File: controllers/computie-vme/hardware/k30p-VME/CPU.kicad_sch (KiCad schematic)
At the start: 18 parts, among them SW1 ~{RESET}, U1 MC68030RC, U2 74HC14, U3 74HC05

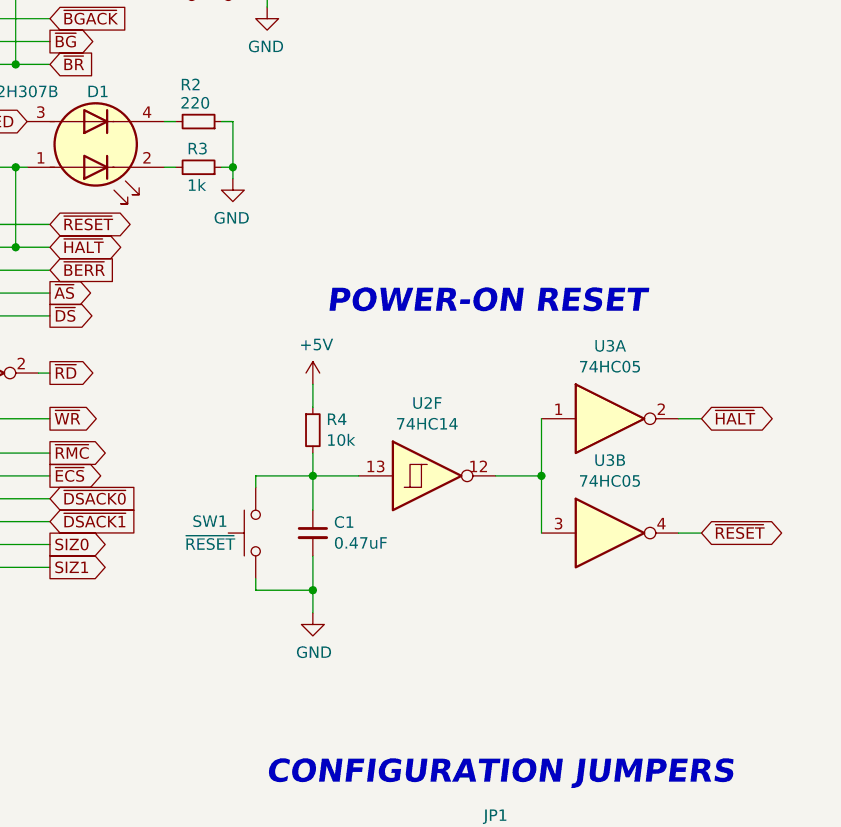
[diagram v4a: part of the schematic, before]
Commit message: Schematics for k30p-VME more or less done
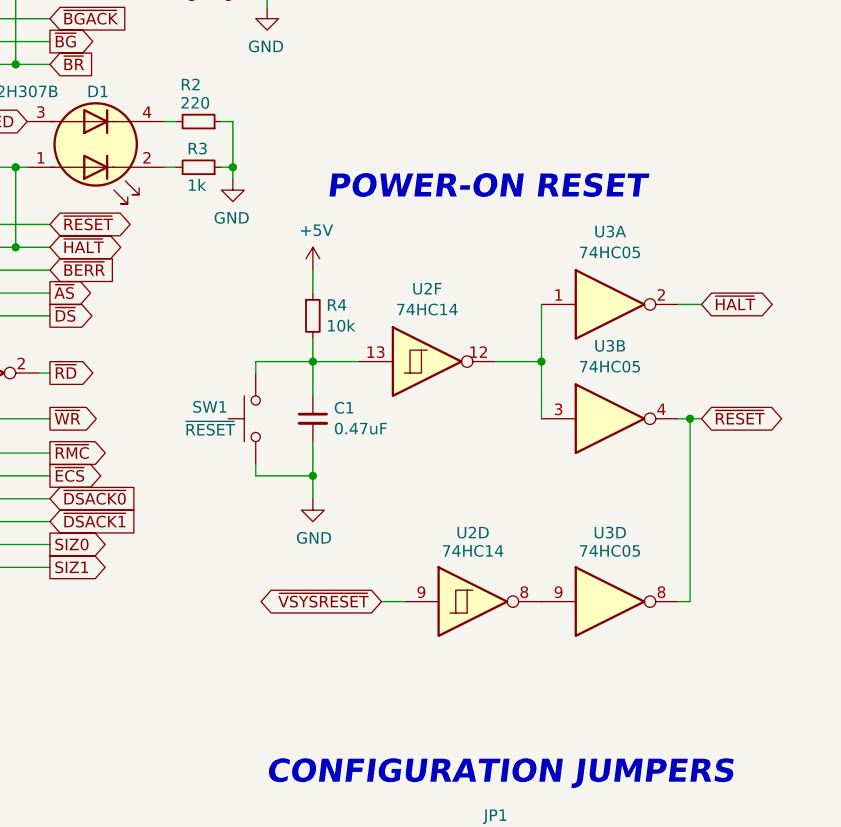
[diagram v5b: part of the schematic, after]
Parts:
- added unit 4 of U2
- added unit 4 of U3
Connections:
- net ~{RESET}: now also U3.8
- new net: U2.8, U3.9
- new net ~{VSYSRESET}: U2.9
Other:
- moved on the sheet: C1, R4, SW1, U2F, U3A, U3B

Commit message: WIP on k30p-VME
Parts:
- removed TP2: IPEND, TestPoint:TestPoint_THTPad_2.0x2.0mm_Drill1.0mm, symbol Connector:TestPoint
- removed TP3: REFILL, TestPoint:TestPoint_THTPad_2.0x2.0mm_Drill1.0mm, symbol Connector:TestPoint
- removed TP4: STATUS, TestPoint:TestPoint_THTPad_2.0x2.0mm_Drill1.0mm, symbol Connector:TestPoint
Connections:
- no-connect marks 5 -> 8
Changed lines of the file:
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@@
 	)
 	(no_connect
+		(at 125.73 142.24)
+	)
+	(no_connect
+		(at 125.73 40.64)
+	)
+	(no_connect
+		(at 125.73 144.78)
+	)
+	(no_connect
 		(at 125.73 100.33)
 	)
@@
 	)
 	(symbol
-		(lib_id "Connector:TestPoint")
-		(at 125.73 40.64 270)
-		(unit 1)
-		(exclude_from_sim no)
-		(in_bom yes)
-		(on_board yes)
-		(dnp no)
-		(property "Reference" "TP2"
-			(at 133.35 40.64 90)
-			(effects
-				(font
-					(size 1.27 1.27)
-				)
-				(justify right)
-			)
-		)
-		(property "Value" "IPEND"
-			(at 127 38.1 90)
-			(effects
-				(font
-					(size 1.27 1.27)
-				)
-				(justify left)
-			)
-		)
-		(property "Footprint" "TestPoint:TestPoint_THTPad_2.0x2.0mm_Drill1.0mm"
-			(at 125.73 45.72 0)
-			(effects
-				(font
-					(size 1.27 1.27)
-				)
-				(hide yes)
-			)
-		)
-		(property "Datasheet" "~"
-			(at 125.73 45.72 0)
-			(effects
-				(font
-					(size 1.27 1.27)
-				)
-				(hide yes)
-			)
-		)
-		(property "Description" ""
-			(at 125.73 40.64 0)
-			(effects
-				(font
-					(size 1.27 1.27)
-				)
-				(hide yes)
-			)
-		)
-		(pin "1"
-		)
-		(instances
-			(project "IVC-k30"
-				(path "/dd13a6b9-cb24-4a73-96ce-c29930072fba/dfc443dd-7c5d-4956-9c53-a8ea419d150b"
-					(reference "TP2")
-					(unit 1)
-				)
-			)
-			(project "k30-SBC"
-				(path "/fc911c32-ec9d-4dc3-a64d-23ac8e8e7030"
-					(reference "TP1")
-					(unit 1)
-				)
-			)
-		)
-	)
-	(symbol
 		(lib_id "Device:R_Small")
 		(at 217.17 60.96 270)
@@
 	)
 	(symbol
-		(lib_id "Connector:TestPoint")
-		(at 125.73 142.24 270)
-		(unit 1)
-		(exclude_from_sim no)
-		(in_bom yes)
-		(on_board yes)
-		(dnp no)
-		(property "Reference" "TP3"
-			(at 133.35 142.24 90)
-			(effects
-				(font
-					(size 1.27 1.27)
-				)
-				(justify right)
-			)
-		)
-		(property "Value" "REFILL"
-			(at 133.35 142.24 90)
-			(effects
-				(font
-					(size 1.27 1.27)
-				)
-				(justify left)
-			)
-		)
-		(property "Footprint" "TestPoint:TestPoint_THTPad_2.0x2.0mm_Drill1.0mm"
-			(at 125.73 147.32 0)
-			(effects
-				(font
-					(size 1.27 1.27)
-				)
-				(hide yes)
-			)
-		)
-		(property "Datasheet" "~"
-			(at 125.73 147.32 0)
-			(effects
-				(font
-					(size 1.27 1.27)
-				)
-				(hide yes)
-			)
-		)
-		(property "Description" ""
-			(at 125.73 142.24 0)
-			(effects
-				(font
-					(size 1.27 1.27)
-				)
-				(hide yes)
-			)
-		)
-		(pin "1"
-		)
-		(instances
-			(project "IVC-k30"
-				(path "/dd13a6b9-cb24-4a73-96ce-c29930072fba/dfc443dd-7c5d-4956-9c53-a8ea419d150b"
-					(reference "TP3")
-					(unit 1)
-				)
-			)
-			(project "k30-SBC"
-				(path "/fc911c32-ec9d-4dc3-a64d-23ac8e8e7030"
-					(reference "TP2")
-					(unit 1)
-				)
-			)
-		)
-	)
-	(symbol
 		(lib_id "Device:LED_Dual_AKAK")
 		(at 205.74 63.5 0)
@@
 					(unit 1)
 				)
-			)
-		)
-	)
-	(symbol
-		(lib_id "Connector:TestPoint")
-		(at 125.73 144.78 270)
-		(unit 1)
-		(exclude_from_sim no)
-		(in_bom yes)
-		(on_board yes)
-		(dnp no)
-		(property "Reference" "TP4"
-			(at 133.35 144.78 90)
-			(effects
-				(font
-					(size 1.27 1.27)
-				)
-				(justify right)
-			)
-		)
-		(property "Value" "STATUS"
-			(at 133.35 144.78 90)
-			(effects
-				(font
-					(size 1.27 1.27)
-				)
-				(justify left)
-			)
-		)
-		(property "Footprint" "TestPoint:TestPoint_THTPad_2.0x2.0mm_Drill1.0mm"
-			(at 125.73 149.86 0)
-			(effects
-				(font
-					(size 1.27 1.27)
-				)
-				(hide yes)
-			)
-		)
-		(property "Datasheet" "~"
-			(at 125.73 149.86 0)
-			(effects
-				(font
-					(size 1.27 1.27)
-				)
-				(hide yes)
-			)
-		)
-		(property "Description" ""
-			(at 125.73 144.78 0)
-			(effects
-				(font
-					(size 1.27 1.27)
-				)
-				(hide yes)
-			)
-		)
-		(pin "1"
-		)
-		(instances
-			(project "IVC-k30"
-				(path "/dd13a6b9-cb24-4a73-96ce-c29930072fba/dfc443dd-7c5d-4956-9c53-a8ea419d150b"
-					(reference "TP4")
-					(unit 1)
-				)
-			)
-			(project "k30-SBC"
-				(path "/fc911c32-ec9d-4dc3-a64d-23ac8e8e7030"
-					(reference "TP3")
-					(unit 1)
-				)

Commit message: k30p-VME PCB work in progress
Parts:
- removed RN1, RN2: 10k, Resistor_THT:R_Array_SIP9, symbol Device:R_Network08
- added RN1, RN2, RN3, RN4: CAT16-103J4LF, Resistor_SMD:R_Cat16-4, symbol Device:R_Pack04
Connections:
- net +5V: now also RN1.5 (R4.2), RN1.6 (R3.2), RN1.7 (R2.2), RN1.8 (R1.2), RN2.5 (R4.2), RN2.6 (R3.2), RN2.7 (R2.2), RN2.8 (R1.2), RN3.5 (R4.2), RN3.6 (R3.2), RN3.7 (R2.2), RN3.8 (R1.2), RN4.5 (R4.2), RN4.6 (R3.2), RN4.7 (R2.2), RN4.8 (R1.2)
- net ~{AVEC}: now also RN1.2 (R2.1)
- net ~{BERR}: now also RN1.3 (R3.1)
- net ~{BGACK}: now also RN1.1 (R1.1)
- net ~{BR}: now also RN3.1 (R1.1)
- net ~{CDIS}: now also RN4.3 (R3.1)
- net ~{DSACK0}: now also RN1.4 (R4.1)
- net ~{DSACK1}: now also RN2.1 (R1.1)
- net ~{IPL0}: now also RN3.3 (R3.1)
- net ~{IPL1}: now also RN3.4 (R4.1)
- net ~{IPL2}: now also RN4.1 (R1.1)
- net ~{MMUDIS}: now also RN4.2 (R2.1)
- net ~{RESET}: now also RN3.2 (R2.1)
- net at U1.G1 (STERM): now also RN2.2 (R2.1)
- net at U1.J1 (CBACK): now also RN2.3 (R3.1)
- net at U1.L1 (CIIN): now also RN2.4 (R4.1)

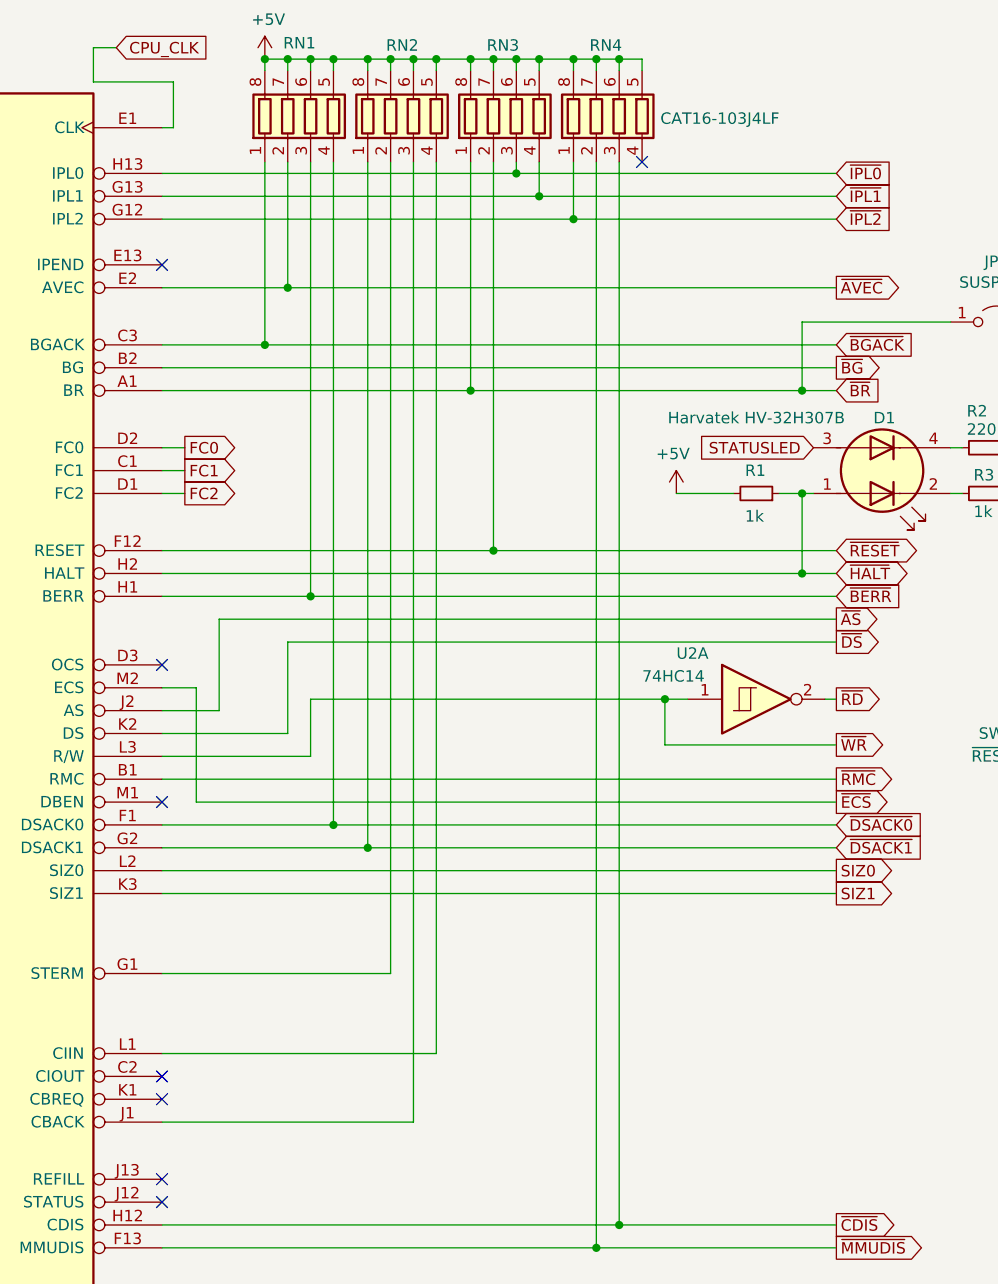
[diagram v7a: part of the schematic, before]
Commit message: Mostly finished k30p-VME board and frontpanel
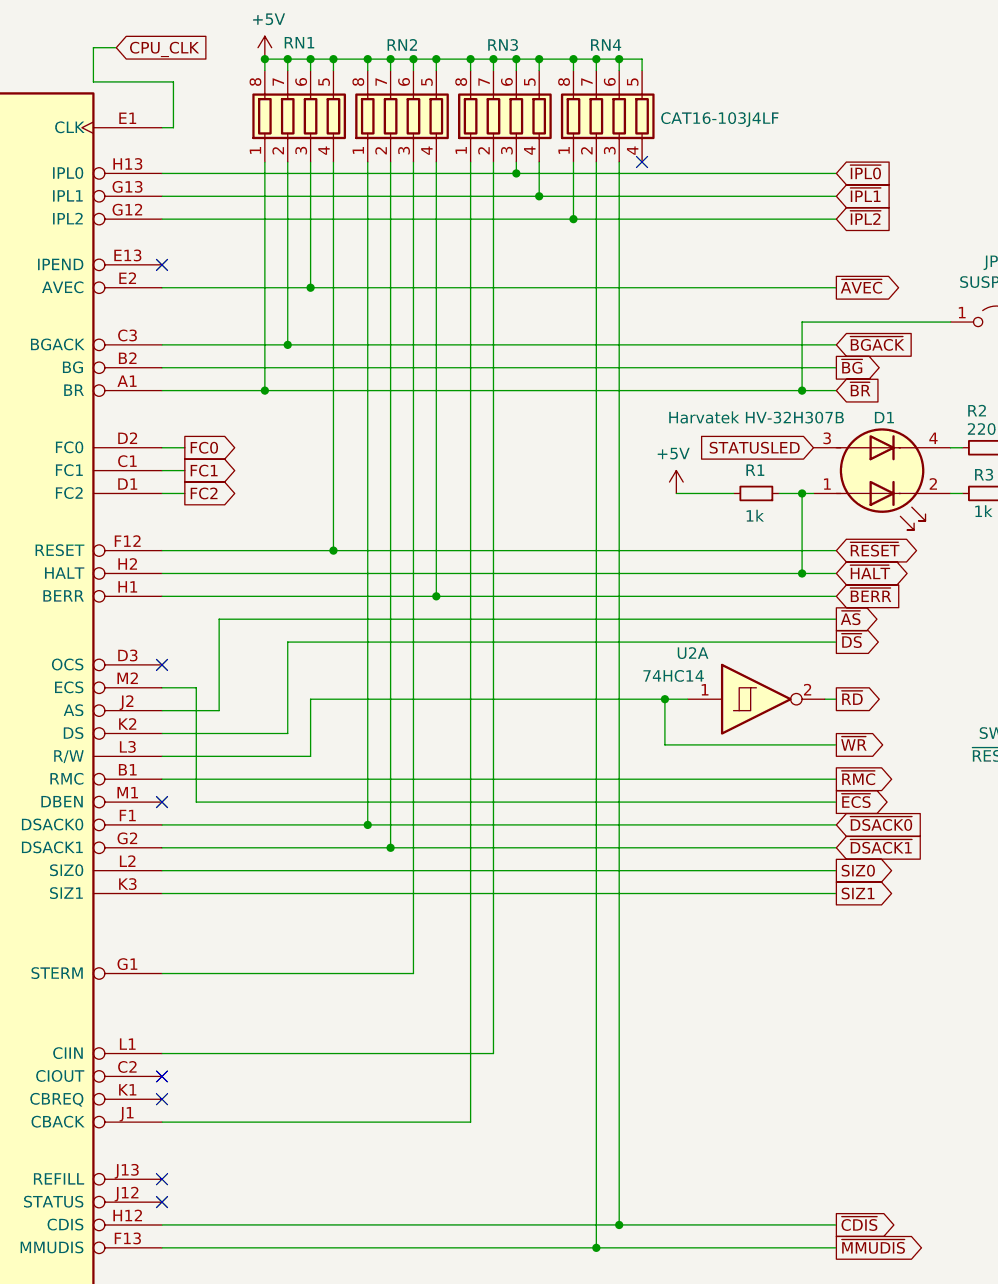
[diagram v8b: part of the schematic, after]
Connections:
- net ~{AVEC}: now also RN1.3 (R3.1); no longer RN1.2 (R2.1)
- net ~{BERR}: now also RN2.4 (R4.1); no longer RN1.3 (R3.1)
- net ~{BGACK}: now also RN1.2 (R2.1); no longer RN1.1 (R1.1)
- net ~{BR}: now also RN1.1 (R1.1); no longer RN3.1 (R1.1)
- net ~{DSACK0}: now also RN2.1 (R1.1); no longer RN1.4 (R4.1)
- net ~{DSACK1}: now also RN2.2 (R2.1); no longer RN2.1 (R1.1)
- net ~{RESET}: now also RN1.4 (R4.1); no longer RN3.2 (R2.1)
- net at U1.G1 (STERM): now also RN2.3 (R3.1); no longer RN2.2 (R2.1)
- net at U1.J1 (CBACK): now also RN3.1 (R1.1); no longer RN2.3 (R3.1)
- net at U1.L1 (CIIN): now also RN3.2 (R2.1); no longer RN2.4 (R4.1)
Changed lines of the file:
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@@
+	)
+	(junction
+		(at 142.24 43.18)
+		(diameter 0)
+		(color 0 0 0 0)
 	)
 	(junction
@@
 	)
 	(junction
+		(at 144.78 72.39)
+		(diameter 0)
+		(color 0 0 0 0)
+	)
+	(junction
 		(at 99.06 191.77)
 		(diameter 0)
@@
 	)
 	(junction
+		(at 137.16 54.61)
+		(diameter 0)
+		(color 0 0 0 0)
+	)
+	(junction
 		(at 151.13 17.78)
 		(diameter 0)
@@
 	)
 	(junction
-		(at 160.02 54.61)
-		(diameter 0)
-		(color 0 0 0 0)
-	)
-	(junction
 		(at 81.28 17.78)
 		(diameter 0)
@@
 	)
 	(junction
-		(at 144.78 102.87)
+		(at 139.7 49.53)
+		(diameter 0)
+		(color 0 0 0 0)
+	)
+	(junction
+		(at 156.21 77.47)
 		(diameter 0)
 		(color 0 0 0 0)
@@
 	)
 	(junction
+		(at 151.13 105.41)
+		(diameter 0)
+		(color 0 0 0 0)
+	)
+	(junction
 		(at 83.82 17.78)
 		(diameter 0)
@@
 	)
 	(junction
+		(at 148.59 102.87)
+		(diameter 0)
+		(color 0 0 0 0)
+	)
+	(junction
 		(at 78.74 191.77)
 		(diameter 0)
@@
 	)
 	(junction
-		(at 148.59 105.41)
-		(diameter 0)
-		(color 0 0 0 0)
-	)
-	(junction
 		(at 93.98 17.78)
 		(diameter 0)
@@
 	)
 	(junction
-		(at 139.7 43.18)
-		(diameter 0)
-		(color 0 0 0 0)
-	)
-	(junction
 		(at 173.99 17.78)
 		(diameter 0)
@@
 	(junction
 		(at 229.87 100.33)
-		(diameter 0)
-		(color 0 0 0 0)
-	)
-	(junction
-		(at 137.16 49.53)
-		(diameter 0)
-		(color 0 0 0 0)
-	)
-	(junction
-		(at 162.56 72.39)
-		(diameter 0)
-		(color 0 0 0 0)
-	)
-	(junction
-		(at 142.24 77.47)
 		(diameter 0)
 		(color 0 0 0 0)
@@
 	(wire
 		(pts
-			(xy 125.73 102.87) (xy 144.78 102.87)
+			(xy 125.73 102.87) (xy 148.59 102.87)
 		)
 		(stroke
@@
 	(wire
 		(pts
-			(xy 151.13 29.21) (xy 151.13 119.38)
+			(xy 153.67 29.21) (xy 153.67 119.38)
 		)
 		(stroke
@@
 	(wire
 		(pts
-			(xy 144.78 29.21) (xy 144.78 102.87)
+			(xy 148.59 29.21) (xy 148.59 102.87)
 		)
 		(stroke
@@
 	(wire
 		(pts
-			(xy 153.67 135.89) (xy 153.67 29.21)
+			(xy 160.02 135.89) (xy 160.02 29.21)
 		)
 		(stroke
@@
 	(wire
 		(pts
-			(xy 148.59 29.21) (xy 148.59 105.41)
+			(xy 151.13 29.21) (xy 151.13 105.41)
 		)
 		(stroke
@@
 	(wire
 		(pts
+			(xy 139.7 49.53) (xy 200.66 49.53)
+		)
+		(stroke
+			(width 0)
+			(type default)
+		)
+	)
+	(wire
+		(pts
 			(xy 45.72 31.75) (xy 54.61 31.75)
 		)
@@
 	(wire
 		(pts
-			(xy 151.13 119.38) (xy 125.73 119.38)
+			(xy 125.73 119.38) (xy 153.67 119.38)
 		)
 		(stroke
@@
 	(wire
 		(pts
-			(xy 139.7 29.21) (xy 139.7 43.18)
+			(xy 142.24 29.21) (xy 142.24 43.18)
 		)
 		(stroke
@@
 	(wire
 		(pts
-			(xy 142.24 77.47) (xy 200.66 77.47)
-		)
-		(stroke
-			(width 0)
-			(type default)
-		)
-	)
-	(wire
-		(pts
 			(xy 153.67 17.78) (xy 156.21 17.78)
 		)
@@
 	(wire
 		(pts
+			(xy 151.13 105.41) (xy 200.66 105.41)
+		)
+		(stroke
+			(width 0)
+			(type default)
+		)
+	)
+	(wire
+		(pts
 			(xy 39.37 180.34) (xy 54.61 180.34)
 		)
@@
 	(wire
 		(pts
+			(xy 144.78 72.39) (xy 200.66 72.39)
+		)
+		(stroke
+			(width 0)
+			(type default)
+		)
+	)
+	(wire
+		(pts
 			(xy 39.37 129.54) (xy 54.61 129.54)
 		)
@@
 	(wire
 		(pts
-			(xy 148.59 105.41) (xy 200.66 105.41)
-		)
-		(stroke
-			(width 0)
-			(type default)
-		)
-	)
-	(wire
-		(pts
 			(xy 39.37 134.62) (xy 54.61 134.62)
 		)
@@
 	(wire
 		(pts
-			(xy 125.73 128.27) (xy 156.21 128.27)
-		)
-		(stroke
-			(width 0)
-			(type default)
-		)
-	)
-	(wire
-		(pts
-			(xy 137.16 49.53) (xy 137.16 29.21)
+			(xy 125.73 128.27) (xy 162.56 128.27)
+		)
+		(stroke
+			(width 0)
+			(type default)
+		)
+	)
+	(wire
+		(pts
+			(xy 139.7 49.53) (xy 139.7 29.21)
 		)
 		(stroke
@@
 	(wire
 		(pts
-			(xy 142.24 77.47) (xy 142.24 29.21)
+			(xy 156.21 77.47) (xy 156.21 29.21)
 		)
 		(stroke
@@
 	(wire
 		(pts
-			(xy 160.02 29.21) (xy 160.02 54.61)
+			(xy 137.16 29.21) (xy 137.16 54.61)
 		)
 		(stroke
@@
 	(wire
 		(pts
+			(xy 137.16 54.61) (xy 196.85 54.61)
+		)
+		(stroke
+			(width 0)
+			(type default)
+		)
+	)
+	(wire
+		(pts
 			(xy 45.72 36.83) (xy 54.61 36.83)
 		)
@@
 	(wire
 		(pts
-			(xy 139.7 43.18) (xy 200.66 43.18)
-		)
-		(stroke
-			(width 0)
-			(type default)
-		)
-	)
-	(wire
-		(pts
 			(xy 125.73 74.93) (xy 196.85 74.93)
 		)
@@
 		)
 	)
-	(wire
-		(pts
-			(xy 160.02 54.61) (xy 196.85 54.61)
-		)
-		(stroke
-			(width 0)
-			(type default)
-		)
-	)
 	(bus
 		(pts
@@
 	(wire
 		(pts
-			(xy 125.73 43.18) (xy 139.7 43.18)
+			(xy 125.73 43.18) (xy 142.24 43.18)
 		)
 		(stroke
@@
 		)
 	)
-	(wire
-		(pts
-			(xy 137.16 49.53) (xy 200.66 49.53)
-		)
-		(stroke
-			(width 0)
-			(type default)
-		)
-	)
 	(bus
 		(pts
@@
 	(wire
 		(pts
+			(xy 156.21 77.47) (xy 200.66 77.47)
+		)
+		(stroke
+			(width 0)
+			(type default)
+		)
+	)
+	(wire
+		(pts
 			(xy 39.37 137.16) (xy 54.61 137.16)
 		)
@@
 	(wire
 		(pts
-			(xy 125.73 54.61) (xy 160.02 54.61)
+			(xy 125.73 54.61) (xy 137.16 54.61)
 		)
 		(stroke
@@
 	(wire
 		(pts
-			(xy 125.73 135.89) (xy 153.67 135.89)
+			(xy 125.73 135.89) (xy 160.02 135.89)
+		)
+		(stroke
+			(width 0)
+			(type default)
+		)
+	)
+	(wire
+		(pts
+			(xy 148.59 102.87) (xy 200.66 102.87)
 		)
 		(stroke
@@
 	(wire
 		(pts
-			(xy 125.73 49.53) (xy 137.16 49.53)
+			(xy 125.73 49.53) (xy 139.7 49.53)
 		)
 		(stroke
@@
 	(wire
 		(pts
+			(xy 142.24 43.18) (xy 200.66 43.18)
+		)
+		(stroke
+			(width 0)
+			(type default)
+		)
+	)
+	(wire
+		(pts
 			(xy 167.64 17.78) (xy 171.45 17.78)
 		)
@@
 	(wire
 		(pts
-			(xy 125.73 77.47) (xy 142.24 77.47)
+			(xy 125.73 77.47) (xy 156.21 77.47)
 		)
 		(stroke
@@
 	(wire
 		(pts
-			(xy 125.73 105.41) (xy 148.59 105.41)
+			(xy 125.73 105.41) (xy 151.13 105.41)
 		)
 		(stroke
@@
 	(wire
 		(pts
-			(xy 156.21 29.21) (xy 156.21 128.27)
+			(xy 162.56 29.21) (xy 162.56 128.27)
 		)
 		(stroke
@@
 	(wire
 		(pts
-			(xy 125.73 72.39) (xy 162.56 72.39)
+			(xy 125.73 72.39) (xy 144.78 72.39)
 		)
 		(stroke
@@
 	(wire
 		(pts
-			(xy 162.56 29.21) (xy 162.56 72.39)
+			(xy 144.78 29.21) (xy 144.78 72.39)
 		)
 		(stroke
@@
 	(wire
 		(pts
-			(xy 162.56 72.39) (xy 200.66 72.39)
-		)
-		(stroke
-			(width 0)
-			(type default)
-		)
-	)
-	(wire
-		(pts
 			(xy 45.72 72.39) (xy 54.61 72.39)
 		)
@@
 		)
 		(stroke
-			(width 0)
-			(type default)
-		)
-	)
-	(wire
-		(pts
-			(xy 144.78 102.87) (xy 200.66 102.87)
-		)
-		(stroke
